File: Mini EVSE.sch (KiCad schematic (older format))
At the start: 12 parts

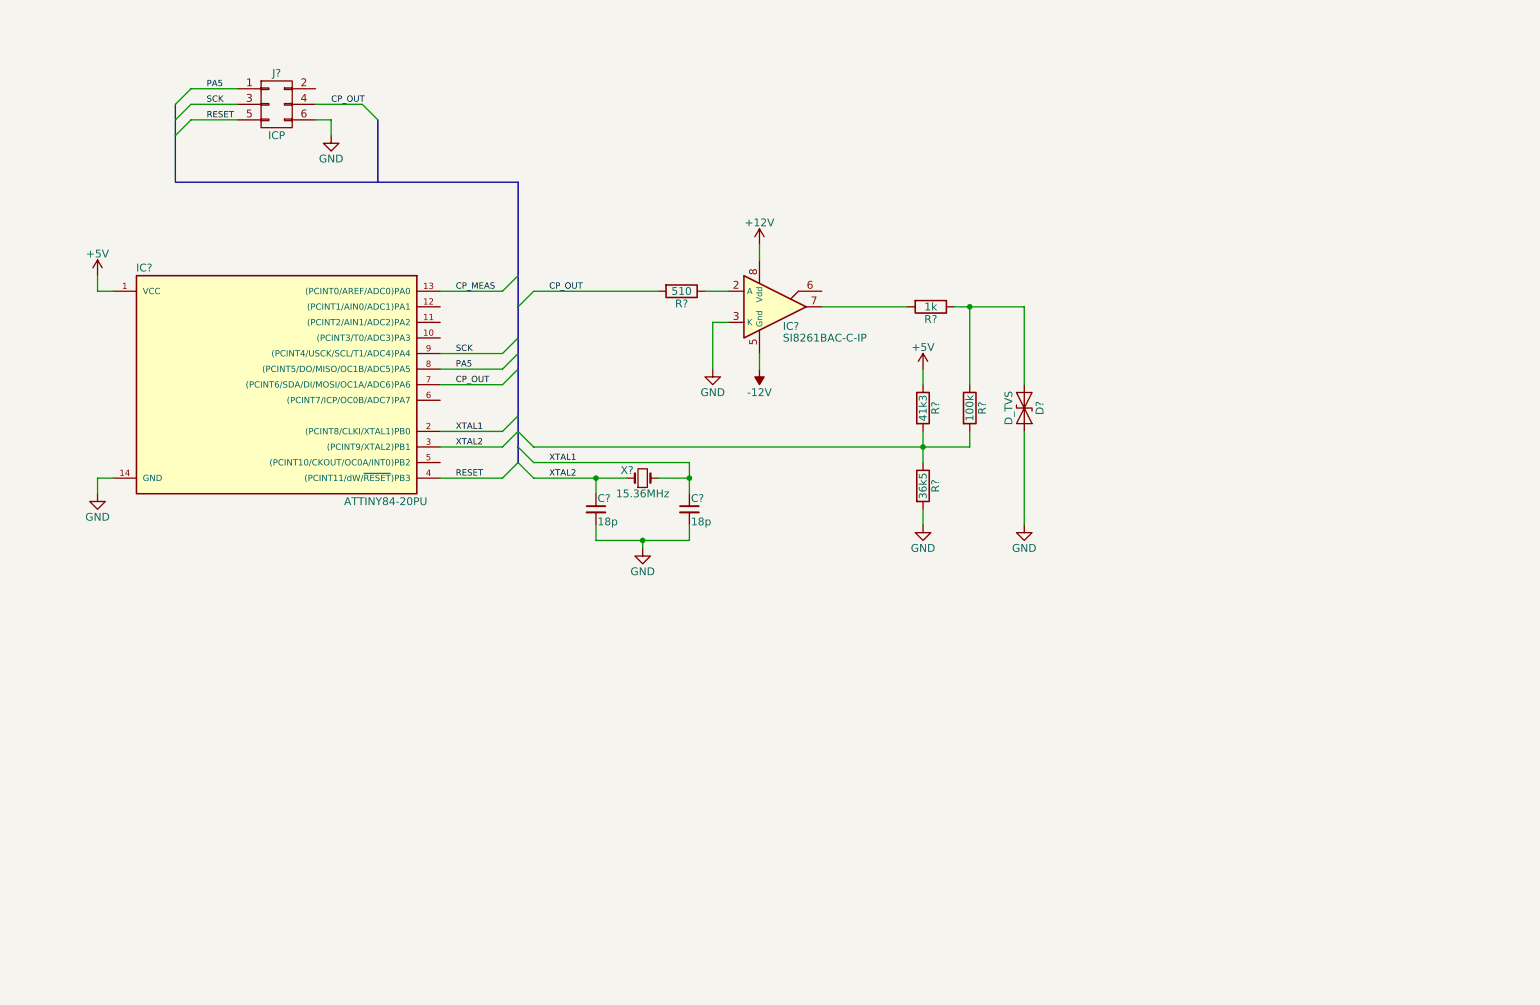
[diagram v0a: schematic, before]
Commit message: Added PSU
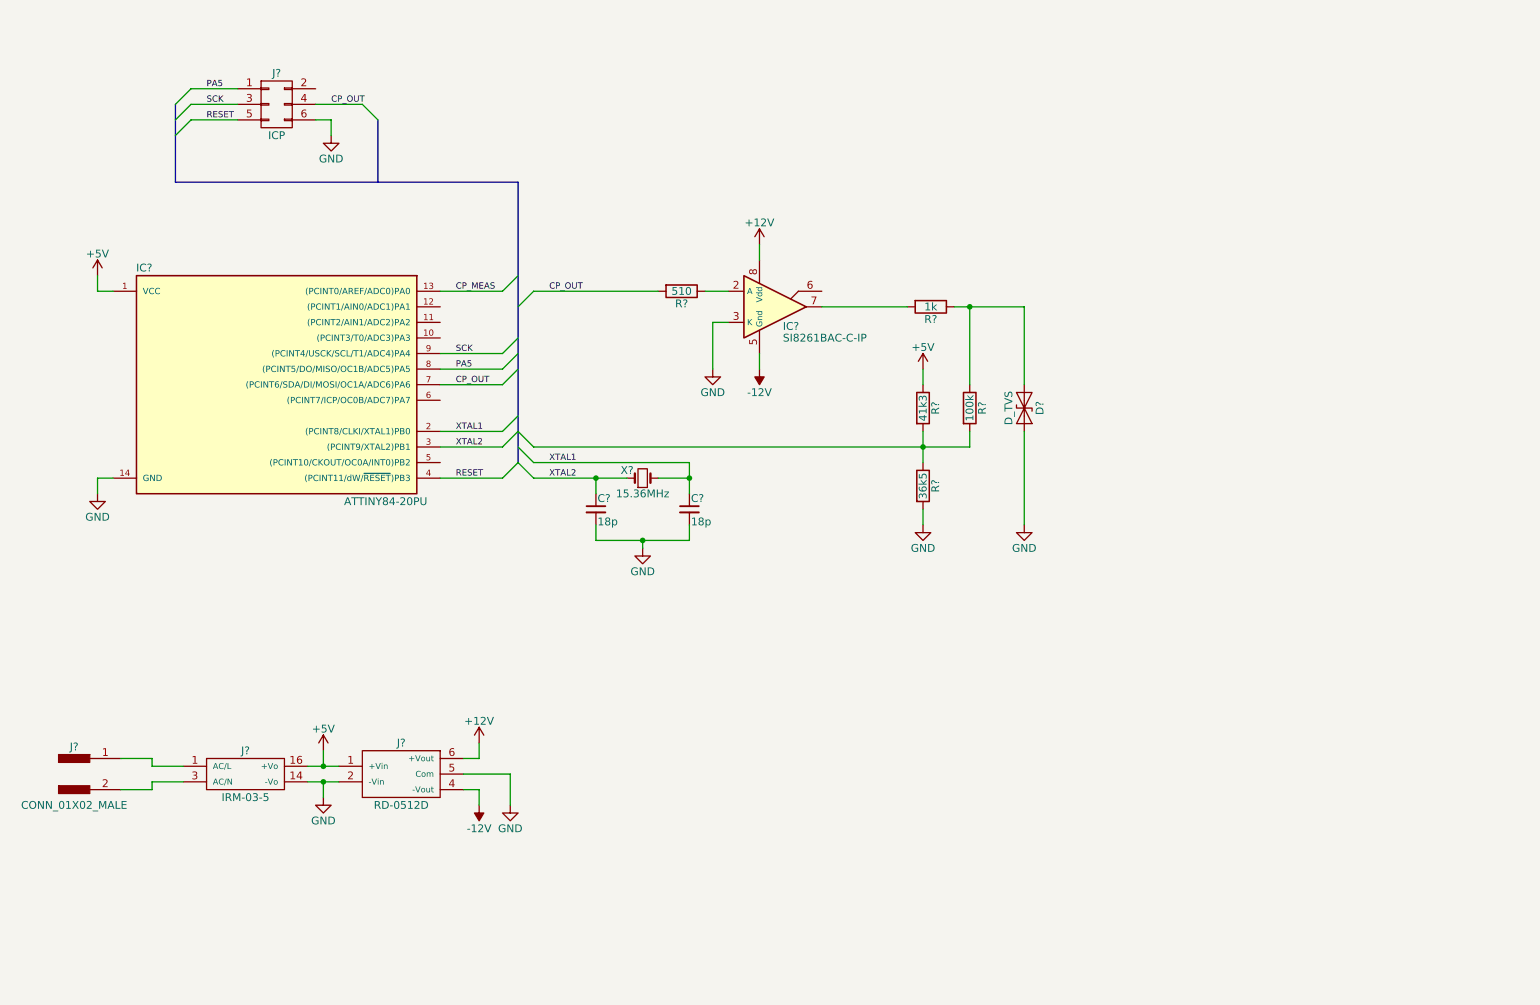
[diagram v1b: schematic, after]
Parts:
- added J?: CONN_01X02_MALE, symbol CONN_01X02_MALE
- added J?: IRM-03-5, symbol IRM-03-5
- added J?: RD-0512D, symbol RD-0512D
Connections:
- net +12V: now also J?.6 (+Vout)
- net +5V: now also J?.1 (+Vin), J?.16 (+Vo)
- net -12V: now also J?.4 (-Vout)
- net GND: now also J?.14 (-Vo), J?.2 (-Vin), J?.5 (Com)
- new net: J?.1, J?.1 (AC/L)
- new net: J?.2, J?.3 (AC/N)
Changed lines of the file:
@@
 LIBS:contrib
 LIBS:valves
+LIBS:Mini EVSE-cache
 EELAYER 25 0
 EELAYER END
@@
 	4900 3800 5100 3800
 Wire Wire Line
-	5100 3700 5100 3800
-Wire Wire Line
-	5100 3800 5100 3900
+	5100 3700 5100 3900
 $Comp
 L GND #PWR?
@@
 	5100 4200 5100 4100
 Wire Wire Line
-	4500 4200 4800 4200
-Wire Wire Line
-	4800 4200 5100 4200
+	4500 4200 5100 4200
 Wire Wire Line
 	4800 4200 4800 4250
@@
 	5950 2700 6500 2700
 Wire Wire Line
-	6800 2700 6900 2700
-Wire Wire Line
-	6900 2700 7250 2700
+	6800 2700 7250 2700
 Wire Wire Line
 	7250 2700 7250 3200
@@
 	1300 3800 1300 3900
 Wire Wire Line
-	4100 3800 4500 3800
-Wire Wire Line
-	4500 3800 4700 3800
+	4100 3800 4700 3800
 Wire Wire Line
 	5100 3700 4100 3700
@@
 $EndComp
 Wire Bus Line
-	4000 1900 4000 2700
-Wire Bus Line
-	4000 2700 4000 2900
-Wire Bus Line
-	4000 2900 4000 3000
-Wire Bus Line
-	4000 3000 4000 3100
-Wire Bus Line
-	4000 3100 4000 3400
-Wire Bus Line
-	4000 3400 4000 3500
-Wire Bus Line
-	4000 3500 4000 3600
-Wire Bus Line
-	4000 3600 4000 3700
+	4000 1900 4000 3700
 Wire Bus Line
 	1800 1900 4000 1900
 Wire Bus Line
-	1800 1400 1800 1500
-Wire Bus Line
-	1800 1500 1800 1600
-Wire Bus Line
-	1800 1600 1800 1900
+	1800 1400 1800 1900
 Wire Bus Line
 	3100 1900 3100 1500
@@
 	6600 4000 6600 4100
 Wire Wire Line
-	6600 3500 6600 3600
-Wire Wire Line
-	6600 3600 6600 3700
+	6600 3500 6600 3700
 Wire Wire Line
 	6900 3600 6900 3500
 Wire Wire Line
-	4100 3600 6600 3600
-Wire Wire Line
-	6600 3600 6900 3600
+	4100 3600 6900 3600
 Connection ~ 6600 3600
 Entry Wire Line
@@
 Wire Wire Line
 	7250 3500 7250 4100
+$Comp
+L CONN_01X02_MALE J?
+U 1 1 59A6EABE
+P 1150 5700
+F 0 "J?" H 1150 5875 50  0000 C CNN
+F 1 "CONN_01X02_MALE" H 1150 5500 50  0000 C CNN
+F 2 "" H 1150 5800 50  0001 C CNN
+F 3 "" H 1150 5800 50  0001 C CNN
+	1    1150 5700
+	1    0    0    -1
+$EndComp
+$Comp
+L IRM-03-5 J?
+U 1 1 59A6ED36
+P 2250 5700
+F 0 "J?" H 2250 5850 50  0000 C CNN
+F 1 "IRM-03-5" H 2250 5550 50  0000 C CNN
+F 2 "" H 2250 5700 50  0001 C CNN
+F 3 "" H 2250 5700 50  0001 C CNN
+	1    2250 5700
+	1    0    0    -1
+$EndComp
+Wire Wire Line
+	1450 5600 1650 5600
+Wire Wire Line
+	1650 5600 1650 5650
+Wire Wire Line
+	1650 5650 1850 5650
+Wire Wire Line
+	1450 5800 1650 5800
+Wire Wire Line
+	1650 5800 1650 5750
+Wire Wire Line
+	1650 5750 1850 5750
+$Comp
+L +5V #PWR?
+U 1 1 59A6EE05
+P 2750 5550
+F 0 "#PWR?" H 2750 5400 50  0001 C CNN
+F 1 "+5V" H 2750 5690 50  0000 C CNN
+F 2 "" H 2750 5550 50  0001 C CNN
+F 3 "" H 2750 5550 50  0001 C CNN
+	1    2750 5550
+	1    0    0    -1
+$EndComp
+Wire Wire Line
+	2650 5650 2850 5650
+Wire Wire Line
+	2750 5650 2750 5550
+$Comp
+L GND #PWR?
+U 1 1 59A6EE81
+P 2750 5850
+F 0 "#PWR?" H 2750 5600 50  0001 C CNN
+F 1 "GND" H 2750 5700 50  0000 C CNN
+F 2 "" H 2750 5850 50  0001 C CNN
+F 3 "" H 2750 5850 50  0001 C CNN
+	1    2750 5850
+	1    0    0    -1
+$EndComp
+Wire Wire Line
+	2650 5750 2850 5750
+Wire Wire Line
+	2750 5750 2750 5850
+$Comp
+L RD-0512D J?
+U 1 1 59A6F2C8
+P 3250 5700
+F 0 "J?" H 3250 5900 50  0000 C CNN
+F 1 "RD-0512D" H 3250 5500 50  0000 C CNN
+F 2 "" H 3250 5700 50  0001 C CNN
+F 3 "" H 3250 5700 50  0001 C CNN
+	1    3250 5700
+	1    0    0    -1
+$EndComp
+Connection ~ 2750 5650
+Connection ~ 2750 5750
+$Comp
+L +12V #PWR?
+U 1 1 59A6F41C
+P 3750 5500
+F 0 "#PWR?" H 3750 5350 50  0001 C CNN
+F 1 "+12V" H 3750 5640 50  0000 C CNN
+F 2 "" H 3750 5500 50  0001 C CNN
+F 3 "" H 3750 5500 50  0001 C CNN
+	1    3750 5500
+	1    0    0    -1
+$EndComp
+$Comp
+L -12V #PWR?
+U 1 1 59A6F44E
+P 3750 5900
+F 0 "#PWR?" H 3750 6000 50  0001 C CNN
+F 1 "-12V" H 3750 6050 50  0000 C CNN
+F 2 "" H 3750 5900 50  0001 C CNN
+F 3 "" H 3750 5900 50  0001 C CNN
+	1    3750 5900
+	-1   0    0    1
+$EndComp
+$Comp
+L GND #PWR?
+U 1 1 59A6F480
+P 3950 5900
+F 0 "#PWR?" H 3950 5650 50  0001 C CNN
+F 1 "GND" H 3950 5750 50  0000 C CNN
+F 2 "" H 3950 5900 50  0001 C CNN
+F 3 "" H 3950 5900 50  0001 C CNN
+	1    3950 5900
+	1    0    0    -1
+$EndComp
+Wire Wire Line
+	3650 5800 3750 5800
+Wire Wire Line
+	3750 5800 3750 5900
+Wire Wire Line
+	3650 5600 3750 5600
+Wire Wire Line
+	3750 5600 3750 5500
+Wire Wire Line
+	3650 5700 3950 5700
+Wire Wire Line
+	3950 5700 3950 5900
 $EndSCHEMATC

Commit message: Project path setup
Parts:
- added C2, C4, C5: 47n, symbol C_Small
- added D2: D_Zener, symbol D_Zener
- added J5: SWITCH, symbol CONN_02X03
- added J6: PILOTS, symbol CONN_01X03_MALE
- added R2, R3, R4: R, symbol R
- added R9: 301, symbol R
- J1: renamed from J?; value CONN_01X02_MALE -> AC IN
- gave numbers to parts that had none: 14
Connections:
- net +12V: now also C4.1
- net +5V: now also C2.1, R9.1
- net -12V: now also C5.1
- net GND: now also C2.2, C4.2, C5.2, D2.2 (A), J5.6 (P6), J6.3
- net LED_R: now reaches IC1.10 ((PCINT3/T0/ADC3)PA3)
- net LED_R: now also R2.2
- net SW: now reaches IC1.11 ((PCINT2/AIN1/ADC2)PA2)
- net SW: now also J5.2 (P2)
- net PP_MEAS: now reaches IC1.12 ((PCINT1/AIN0/ADC1)PA1)
- net PP_MEAS: now also D2.1 (K), J6.1, R9.2
- net LED_B: now reaches IC1.5 ((PCINT10/CKOUT/OC0A/INT0)PB2)
- net LED_B: now also R4.2
- net LED_G: now reaches IC1.6 ((PCINT7/ICP/OC0B/ADC7)PA7)
- net LED_G: now also R3.2
- net at D1.1 (A1), R7.1, R8.1: now also J6.2
- new net: J5.1 (P1), R2.1
- new net: J5.3 (P3), R3.1
- new net: J5.5 (P5), R4.1
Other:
- moved on the sheet: C1, C3, D1, IC1, IC2, J1, J2, J3, J4, R1, R5, R6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

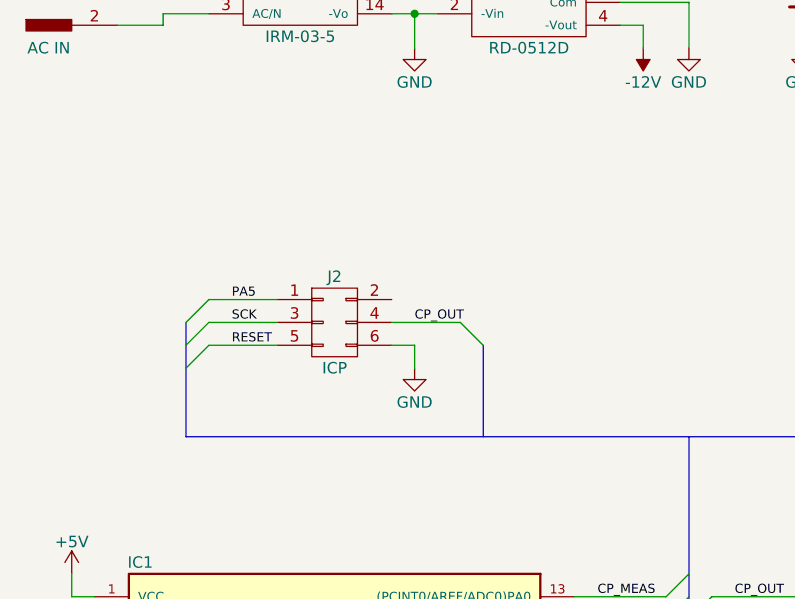
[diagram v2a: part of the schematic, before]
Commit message: Added footprints
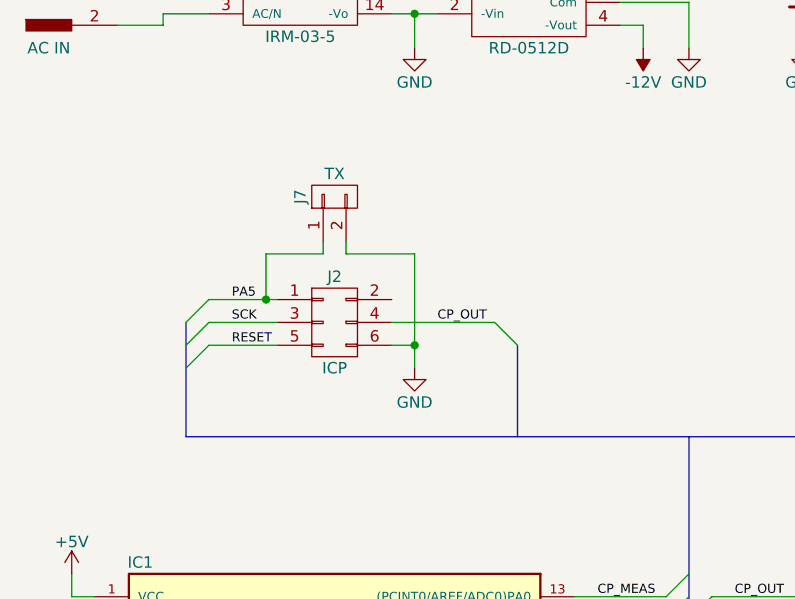
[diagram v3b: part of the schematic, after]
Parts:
- added J7: TX, Pin_Headers:Pin_Header_Straight_1x02_Pitch2.54mm, symbol CONN_01X02
- C1, C3: footprint (none) -> Miscellaneous:C_Disc_D2.5mm_W3.2mm_P2.54mm
- C2, C4, C5: footprint (none) -> Miscellaneous:C_Disc_D5.1mm_W3.2mm_P5.08mm
- D1, D2: footprint (none) -> Diodes_THT:D_DO-201AD_P12.70mm_Horizontal
- IC1: footprint Housings_DIP:DIP-14_W7.62mm -> Housings_DIP:DIP-14_W7.62mm_LongPads
- IC2: footprint (none) -> Housings_DIP:DIP-8_W7.62mm_LongPads
- J1: footprint (none) -> Connectors:bornier2
- J2, J5: footprint (none) -> Pin_Headers:Pin_Header_Straight_2x03_Pitch2.54mm
- J3: footprint (none) -> Miscellaneous:MeanWell_IRM
- J4: footprint (none) -> Miscellaneous:Recom_1x05_Pitch2.54mm
- J6: footprint (none) -> Connectors:bornier3
- R1, R2, R3, R4, R5, R6, R7, R8, R9: footprint (none) -> Miscellaneous:R_Axial_DIN0207_L6.3mm_D2.5mm_P10.16mm_Horizontal
- X1: footprint (none) -> Crystals:Crystal_HC49-U_Vertical
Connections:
- net GND: now also J7.2 (P2)
- net PA5: now also J7.1 (P1)

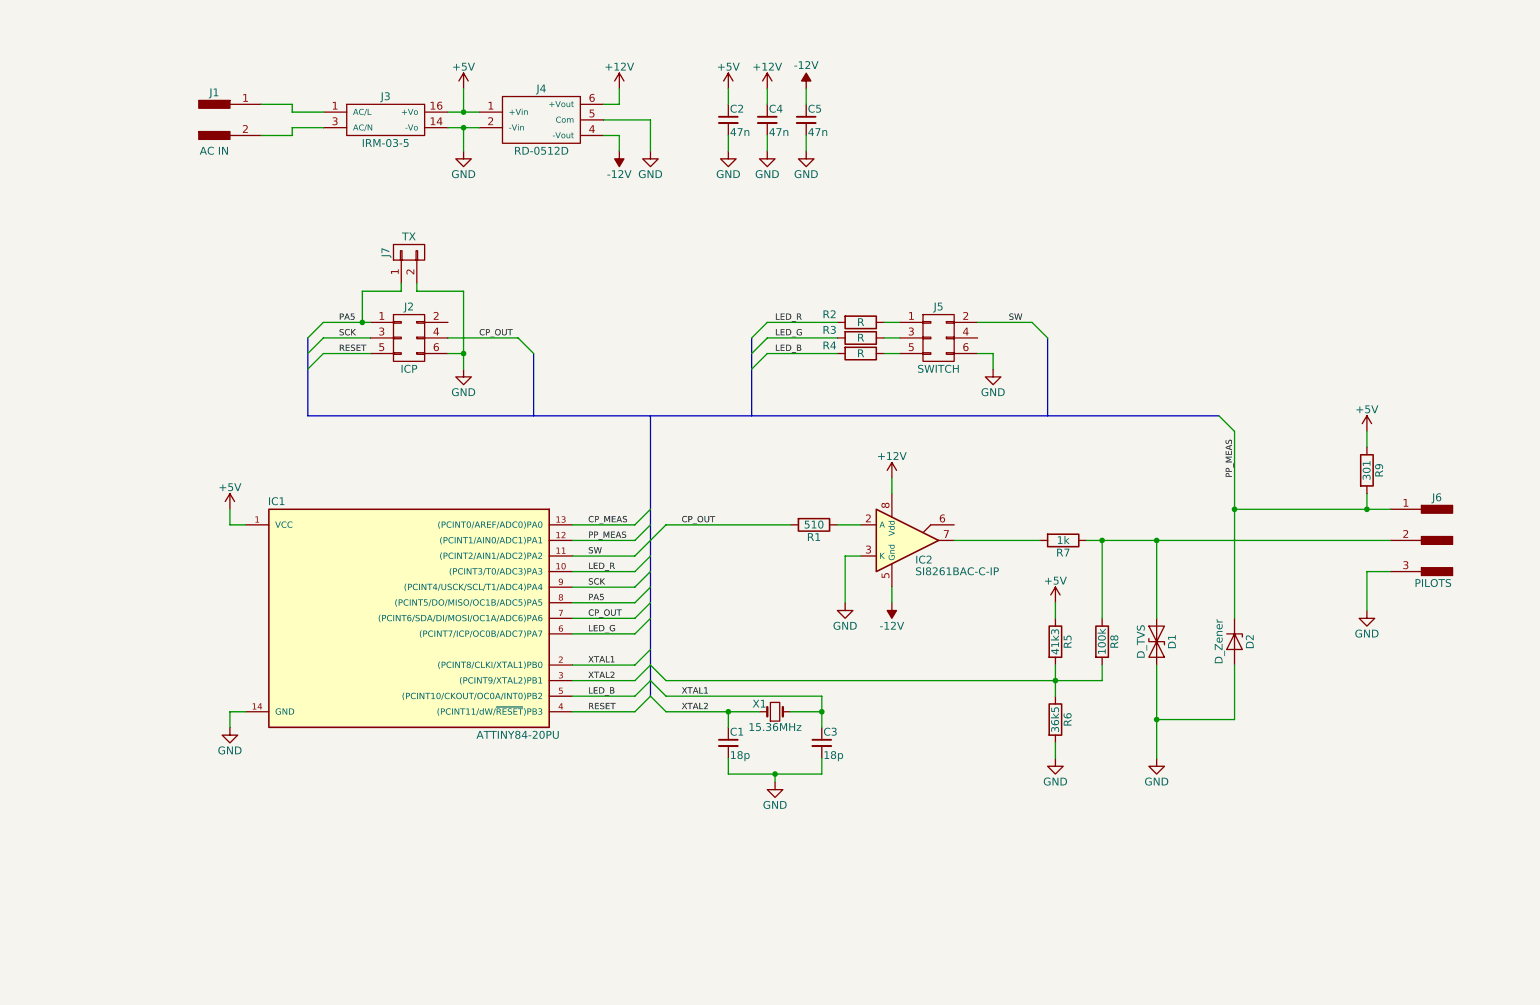
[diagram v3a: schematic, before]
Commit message: Added SSR relay for main contactor
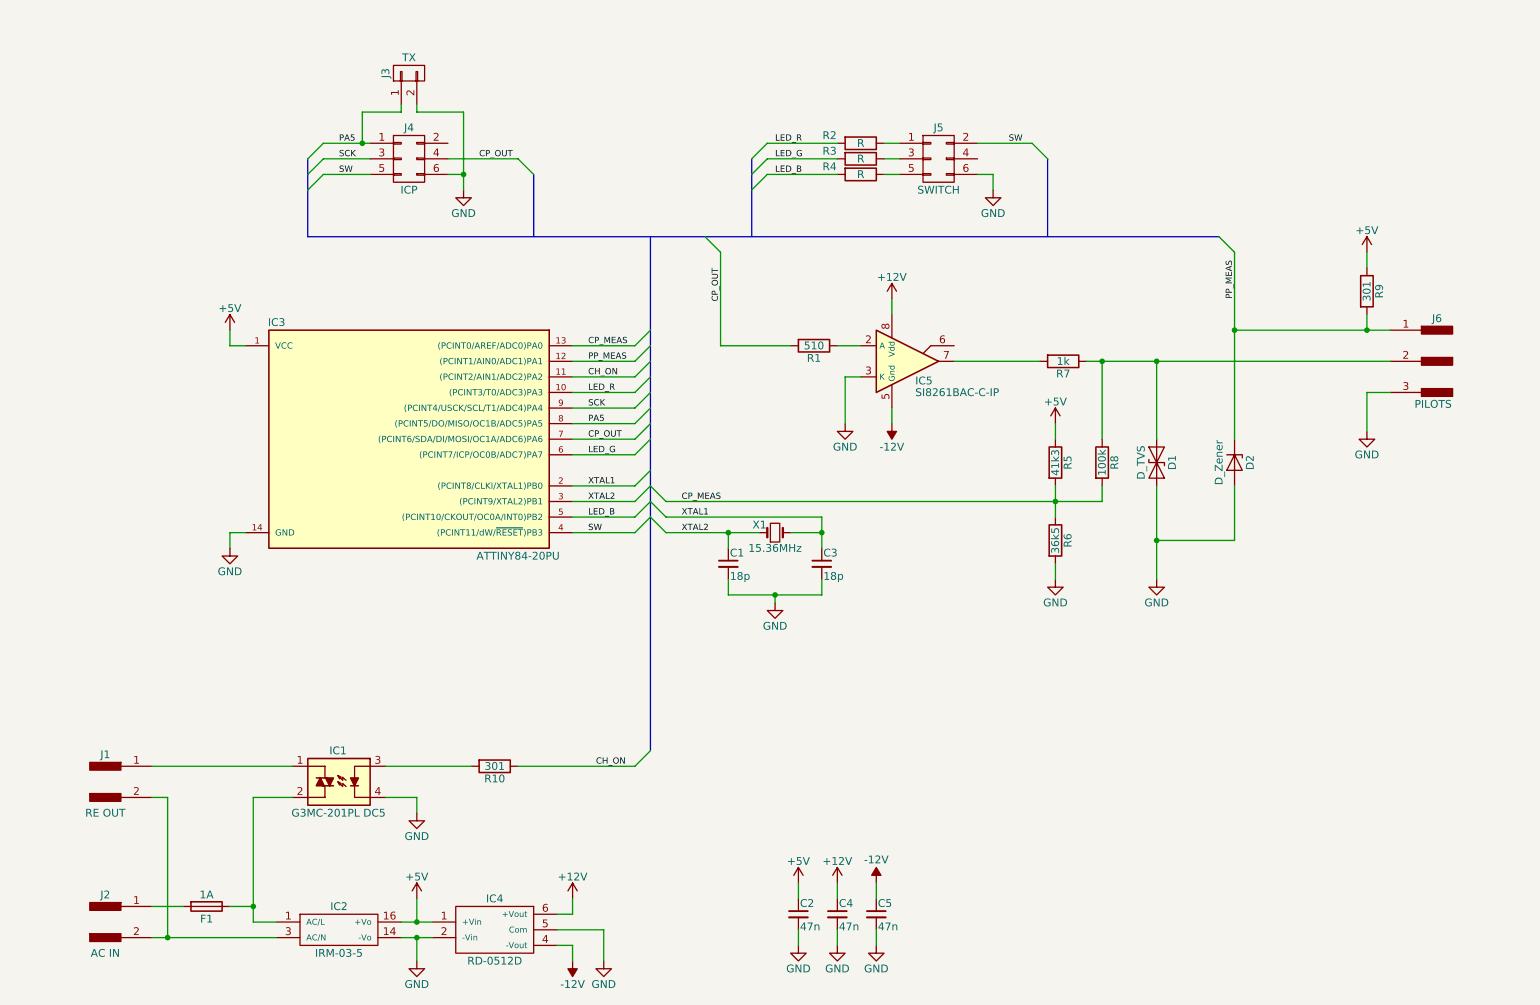
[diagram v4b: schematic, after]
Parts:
- added F1: 1A, Miscellaneous:R_Axial_DIN0207_L6.3mm_D2.5mm_P10.16mm_Horizontal, symbol Fuse
- added IC1: G3MC-201PL DC5, Miscellaneous:SIP4_Omron-SSR_Pitch10.16mm_Straight, symbol S102S01
- added J1: RE OUT, Connectors:bornier2, symbol CONN_01X02_MALE
- added R10: 301, Miscellaneous:R_Axial_DIN0207_L6.3mm_D2.5mm_P10.16mm_Horizontal, symbol R
- renumbered J3 to IC2, IC1 to IC3, J4 to IC4, IC2 to IC5, J1 to J2, J7 to J3, J2 to J4
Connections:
- net RESET is gone; now on net SW: IC3.4 ((PCINT11/dW/~RESET~)PB3), J4.5 (P5)
- net CP_MEAS: now also R5.2, R6.1, R8.2
- net GND: now also IC1.4
- net SW: no longer IC3.11 ((PCINT2/AIN1/ADC2)PA2)
- net at J2.1: now also F1.2; no longer IC2.1 (AC/L)
- net at IC2.3 (AC/N), J2.2: now also J1.2
- new net: F1.1, IC1.2, IC2.1 (AC/L)
- new net: IC1.1, J1.1
- new net: IC1.3, R10.2
- new net CH_ON: IC3.11 ((PCINT2/AIN1/ADC2)PA2), R10.1
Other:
- moved on the sheet: C1, C2, C3, C4, C5, D1, D2, IC2, IC3, IC4, IC5, J2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
